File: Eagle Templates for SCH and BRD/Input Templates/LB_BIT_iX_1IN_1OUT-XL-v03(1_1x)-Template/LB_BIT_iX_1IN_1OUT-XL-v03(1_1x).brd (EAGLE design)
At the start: 21.4 x 38 mm, 17 parts, among them U1 LV321SOT23-5, U2 LV321SOT23-5

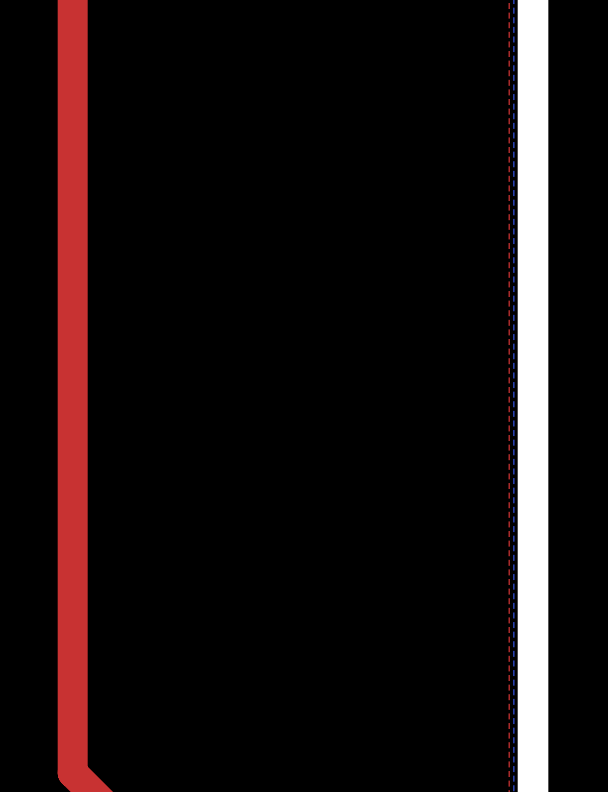
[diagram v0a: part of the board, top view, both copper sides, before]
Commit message: added bitlab logo and made minor changes to board templates. Updated littlebits library.
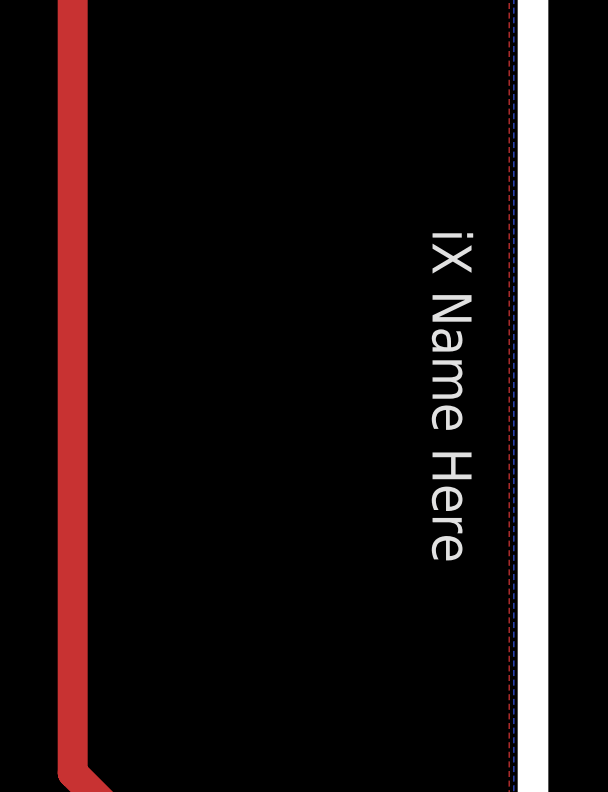
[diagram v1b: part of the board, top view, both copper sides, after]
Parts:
- added U$5: (no value), LITTLEBITS:BITLAB-LOGO
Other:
- board text added: "iX Name Here"
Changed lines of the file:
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@@
 <layer number="113" name="extra" color="10" fill="1" visible="yes" active="yes"/>
 <layer number="116" name="Patch_BOT" color="9" fill="4" visible="yes" active="yes"/>
+<layer number="118" name="Rect_Pads" color="7" fill="1" visible="no" active="yes"/>
 <layer number="121" name="_tsilk" color="7" fill="1" visible="yes" active="yes"/>
 <layer number="122" name="_bsilk" color="7" fill="1" visible="yes" active="yes"/>
@@
 <wire x1="5.78" y1="4.11" x2="2.51" y2="4.11" width="1" layer="46"/>
 <wire x1="2.51" y1="42.125" x2="2.51" y2="4.11" width="1" layer="46"/>
+<text x="21.2" y="23.1" size="1.3" layer="21" font="vector" rot="SR270" align="center">iX Name Here</text>
 </plain>
 <attributes>
@@
 <element name="U$2" library="LITTLEBITS" package="FABDWG01-OHW" value="FRAME-LETTER" x="0" y="0"/>
 <element name="U$4" library="ohw-logo" package="OSHW_FILLX150_NOTEXT" value="" x="18.7" y="35.9" rot="MR90"/>
+<element name="U$5" library="LITTLEBITS" package="BITLAB-LOGO" value="" x="19.7" y="27.5" rot="R270"/>
 </elements>
 <signals>

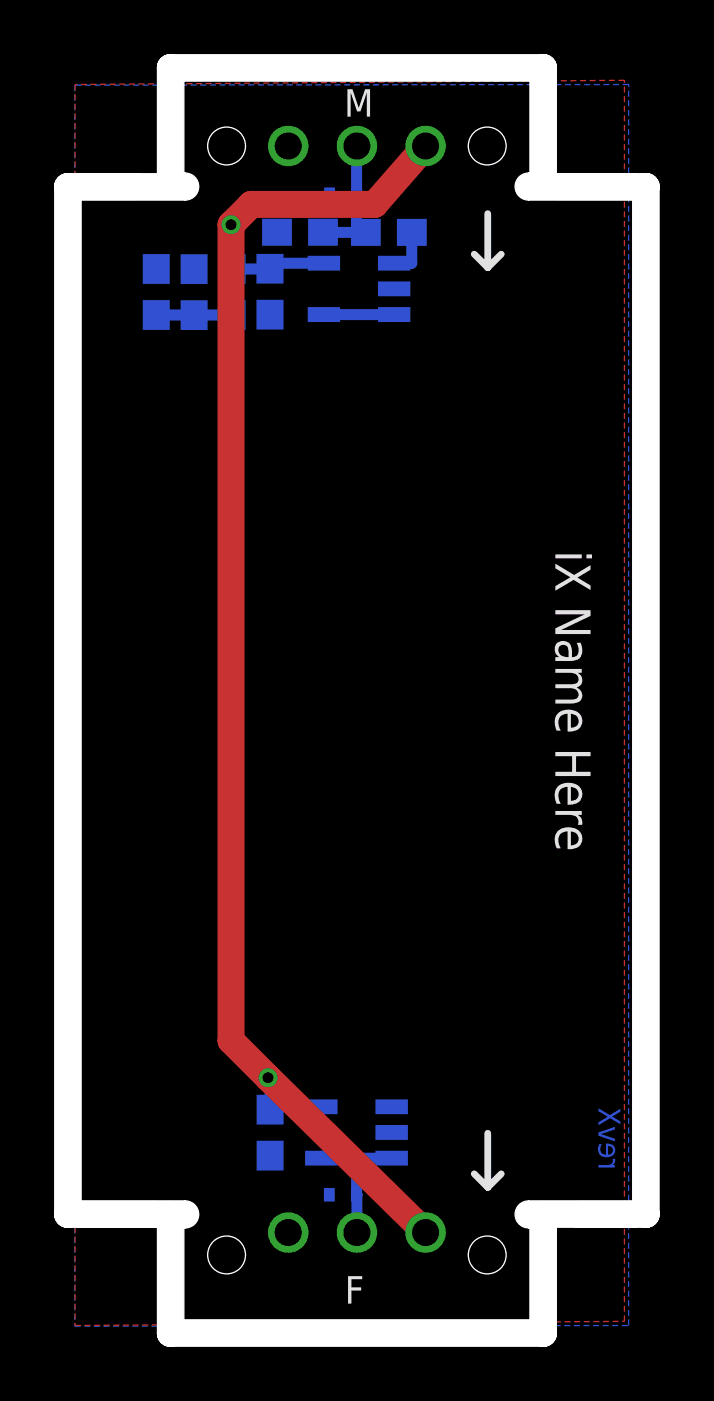
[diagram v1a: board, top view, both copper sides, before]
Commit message: Updated templates
- Added ferrite beads
- Moved text and annotations off of Nets layer
- Minor layout changes
- Removed I/O/W prefix from reference designators
- Removed output stage components from output bits
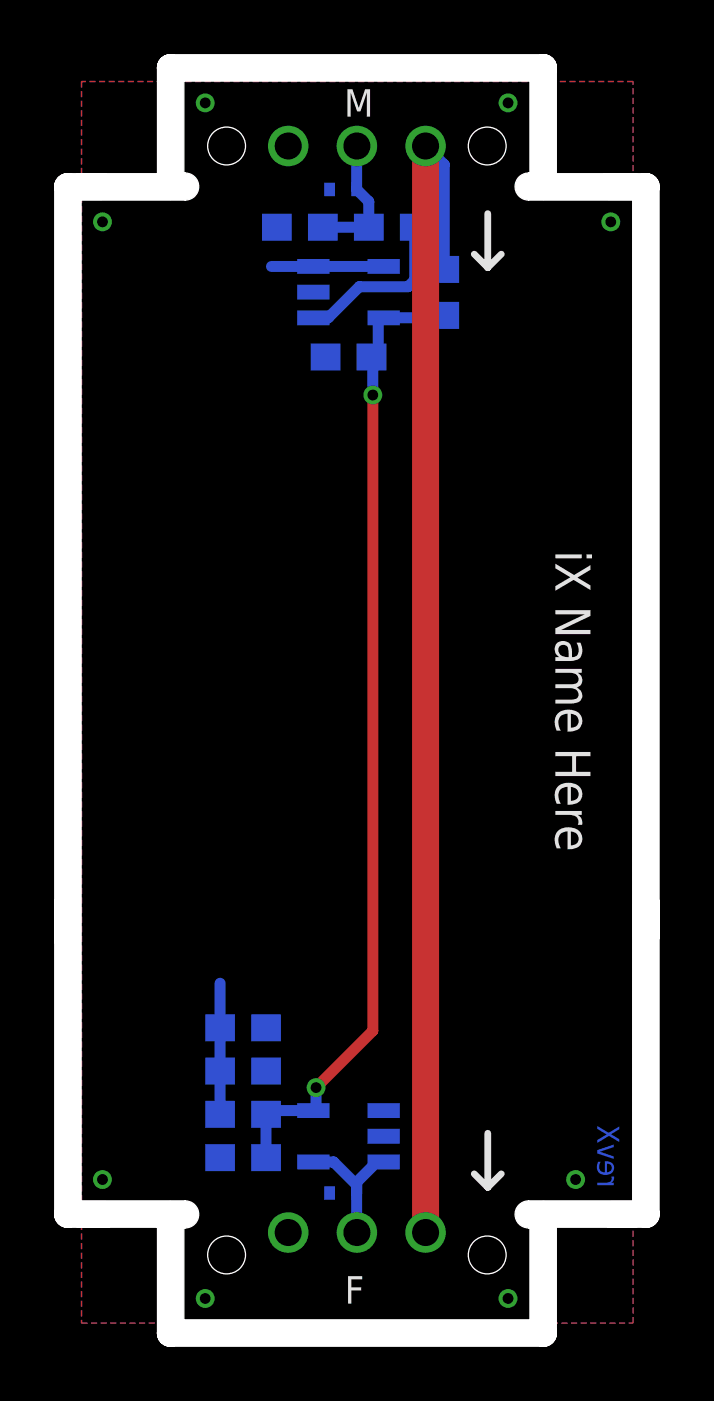
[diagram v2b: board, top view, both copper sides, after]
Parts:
- removed I?C1: 0.1uF, LITTLEBITS:CAP-0603
- removed I?C2: 10uF, LITTLEBITS:CAP-0603
- removed I?C3: 1.0uF, LITTLEBITS:CAP-0603
- removed I?R1: 1meg, LITTLEBITS:RES-0603
- removed I?R2: 10K, LITTLEBITS:RES-0603
- removed I?R3, I?R4: 3K3, LITTLEBITS:RES-0603
- removed I?TVS1, I?TVS2: ESD9B5.0ST5G, LITTLEBITS:SOD-923
- added C1: 0.1uF, LITTLEBITS:CAP-0603
- added C2: 10uF, LITTLEBITS:CAP-0603
- added C3: 1.0uF, LITTLEBITS:CAP-0603
- added FB1: FERRITE-BEAD0603, LITTLEBITS:R0603
- added R1: 1meg, LITTLEBITS:RES-0603
- added R2: 10K, LITTLEBITS:RES-0603
- added R3, R4: 3K3, LITTLEBITS:RES-0603
- added TVS1, TVS2: ESD9B5.0ST5G, LITTLEBITS:SOD-923
- U$2: value FRAME-LETTER -> OSHWCREDIT; device LITTLEBITS:FABDWG01-OHW -> LITTLEBITS:OSHWCREDIT
- U$3: value OSHWCREDIT -> FRAME-LETTER; device LITTLEBITS:OSHWCREDIT -> LITTLEBITS:FABDWG01-OHW
- moved U$2 112.4 mm to (-92.2, -64.3)
- moved U$3 112.1 mm to (0.00, 0.00)
- moved U$1 4.98 mm to (-37.5, -68.2)
- moved U1 0.41 mm to (12.9, 38.2), turned to 90 degrees
- moved U2 0.33 mm to (12.9, 7.00)
- renumbered I?BSF to BSF1, I?BSM to BSM1
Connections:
- removed net N1: BSF1.GND, BSM1.GND1
- new net LB_VCC: BSF1.VCC, BSM1.VCC1, FB1.2
- net GND: now also BSF1.GND, BSM1.GND1, C1.2, C2.2, C3.1, R1.1, R4.1, TVS1.1, TVS2.1; no longer I?C1.2, I?C2.2, I?C3.1, I?R1.1, I?R4.1, I?TVS1.1, I?TVS2.1
- net N$4: now also R2.1; no longer I?R2.1
- net SIG_IN: now also R1.2, R2.2, TVS1.2; no longer I?R1.2, I?R2.2, I?TVS1.2
- net SIG_OUT: now also TVS2.2; no longer I?TVS2.2
- net VCC: now also C1.1, C3.2, FB1.1, R3.2; no longer BSF1.VCC, BSM1.VCC1, I?C1.1, I?C3.2, I?R3.2
- net VREF: now also C2.1, R3.1, R4.2; no longer I?C2.1, I?R3.1, I?R4.2
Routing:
- net LB_VCC: track 0.00 -> 45.0 mm
- net VCC: track 57.3 -> 36.9 mm
- net N$4: track 1.79 -> 6.28 mm
- net VREF: track 2.81 -> 4.85 mm
- net N$2: track 2.60 -> 4.15 mm
- added copper zone on layer 1, net GND
- added copper zone on layer 16, net GND
- removed copper zone on layer 1, net N1
- removed copper zone on layer 16, net N1
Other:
- outline, holes or cut-outs redrawn
